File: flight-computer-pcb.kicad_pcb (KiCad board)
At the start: 4 copper layers, 140 x 80 mm, 4 parts, among them U1 Teensy4.1, U2 BMP390, U3 BNO055, U9 S13V10F5

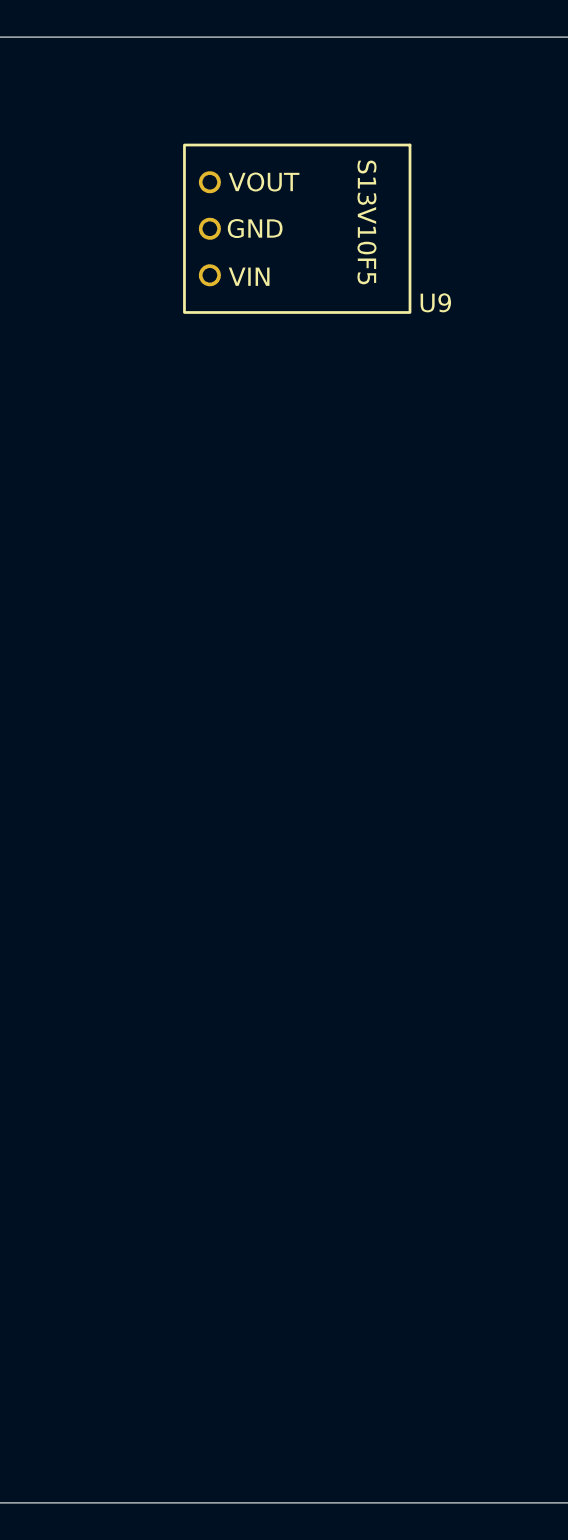
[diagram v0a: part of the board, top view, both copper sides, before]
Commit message: feat: add S7V8F3, U3V16F9, and U3V70F6 footprint to sch and pcb
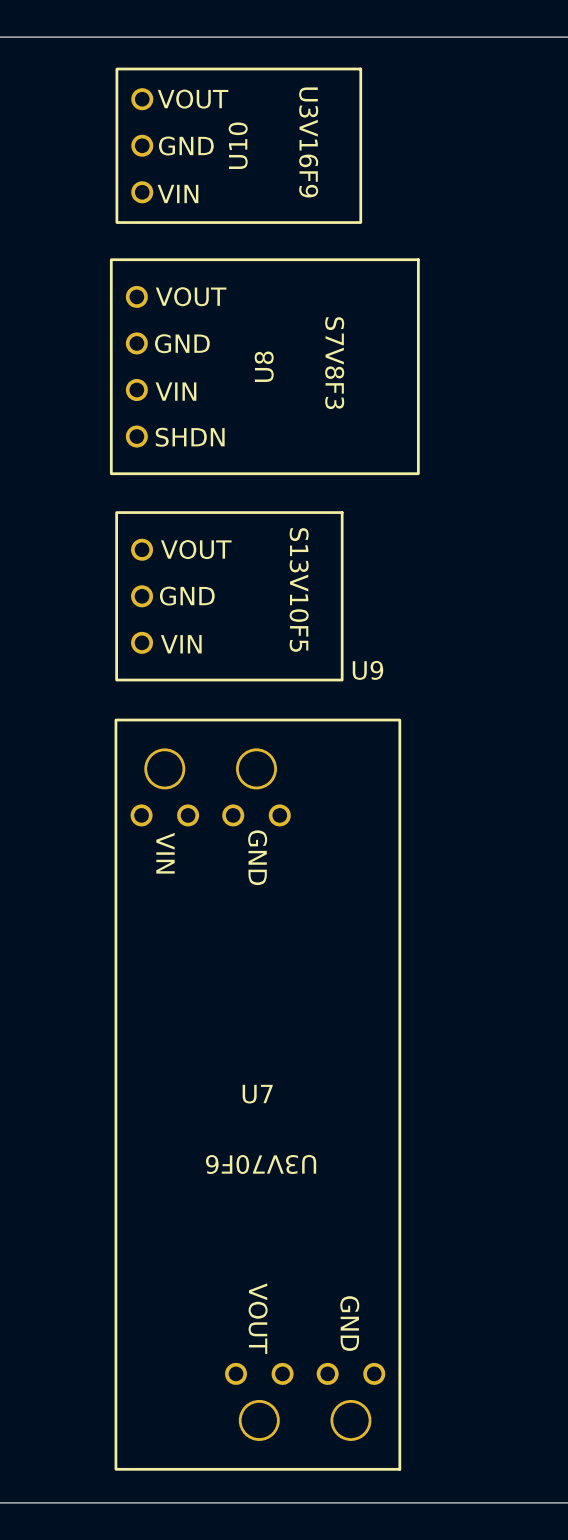
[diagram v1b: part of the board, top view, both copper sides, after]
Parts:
- added U10: U3V16F9, FlightComputer:U3V16F9, F.Cu at (196.6, 65.9)
- added U7: U3V70F6, FlightComputer:U3V70F6, F.Cu at (197.6, 117.7)
- added U8: S7V8F3, FlightComputer:S7V8F3, F.Cu at (198.0, 78.0)
- moved U9 20.4 mm to (196.1, 90.5)
